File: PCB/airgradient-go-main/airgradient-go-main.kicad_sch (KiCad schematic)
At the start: 200 parts, among them CN1 HCZZ0032-5, CN2 HCZZ0032-5, CN3 HCZZ0032-5, Q1 SIA445EDJ-T1-GE3, Q2 ZVN4106FTA_C508255, Q3 CSD83325L, Q4 SS8050-G, Q5 SI1308EDL, SW1 TS-1091C-A1B3-D2, SW2 TS-1091C-A1B3-D2, U1 W25N512GVEIG, U10 SGP41-D-R4, U11 PS1-CO-SMOKE-10k, U12 SHT4x, U13 SPL07-003, U14 LIS2DH12TR, U15 TMUX121NKGR_C22428404, U16 S12, U17 TCA6408ARGT, U18 TAU1113, U19 LM66200DRLR, U2 ZDSD512MLGEAG, U20 LP5036, U3 BQ27742YZFR-G1, U4 ESP32-C5-MINI-1, U5 BQ25628RYKR, U6 HYG-8503A, U7 TPL5010DDCR, U8 TPS63802DLAR, U9 TPS7A0228DQNR

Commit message: Add 32.768 kHz RTC crystal on IO0/IO1, move ePaper CS to TCA6408A P7
- New RTC 32K block: Y1 Epson FC-135R X1A0001410006 (LCSC C94673,
  CL 6 pF, ESR 50 kOhm max) with C76/C77 8.2 pF C0G (C1579) to PGND,
  on U4 pin 16 (IO0 = XTAL_32K_P) and pin 17 (IO1 = XTAL_32K_N).
- ePaper CS leaves U4 IO0 and moves to expander U17 P7; R39 100K
  pull-up keeps the display deselected while the expander resets.
- design/: requirements, part extraction, intent table and block spec
  (schematic-design skill). net_diff 0 errors, ERC 272 -> 270.
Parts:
- added C76, C77: 8.2pF/50V, Capacitor_SMD:C_0402_1005Metric, symbol Device:C
- added Y1: 32.768kHz CL6pF, Crystal:Crystal_SMD_3215-2Pin_3.2x1.5mm, symbol Device:Crystal
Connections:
- net GND: now also C76.2, C77.2
- net ePaper CS: now also U17.10 (P7); no longer U4.16 (IO0)
- net IO1 renamed XTAL_32K_N
- net XTAL_32K_N: now also C77.1, Y1.2
- new net XTAL_32K_P: C76.1, U4.16 (IO0), Y1.1
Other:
- note added: "RTC 32K"
- note added: "Y1 FC-135R CL 6 pF, ESR 50 kOhm max (FC-135R p2) ESP32-C5 limit ESR <= 70 kOhm (MINI-1 Fig 9-1 p49) C76 = C77 = 2 x (CL - Cstray) = 2 x (6 - 2) = 8.2 pF C0G (R-XT-01) XTAL_32K_P/N = U4 IO0/IO1. ePaper CS moved to U17 P7 (R-XT-02)"

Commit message: Lay out the RTC crystal; move ePaper CS to IO4
Schematic: ePaper CS moves from expander P7 to U4 IO4 (pad 8); P7 gets
an NC flag. The P7 route needed 5 vias through EN_PM1/BUZZ/PRTRG.

PCB (pcb-design skill, groups in design/.../layout/route.json):
- Y1/C77/C76 in the column between U4 and U2, next to U4 pads 16/17.
  XTAL_32K_P/N on F.Cu, 0 vias, 4.9/4.5 mm; C77 GND via 0.5/0.3.
- MOSI rerouted out of that column: U4 trunk -> U1.5 above the
  crystal (1 via), U1.5 -> U2.5 on its right side (2 vias).
- ePaper CS from IO4 under the module body to the old trunk (1 via);
  the old IO0 stub and the dead trunk ends are removed.
- Memory silk line split around the crystal; 8 references re-placed.

Checks: DRC 230 = baseline (0 new), 0 unconnected, parity 0. No new
bends, junctions, dangling ends or vias vs HEAD; unrelated nets
identical to HEAD. Accepted: I2C on B.Cu under Y1/C77 (RF-22, GND
plane between), CS at 0.2 mm.
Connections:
- net IO4 is gone; now on net ePaper CS: U4.8 (IO4)
- net ePaper CS: no longer U17.10 (P7)
- no-connect marks 29 -> 30
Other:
- note added: "Y1 FC-135R CL 6 pF, ESR 50 kOhm max (FC-135R p2) ESP32-C5 limit ESR <= 70 kOhm (MINI-1 Fig 9-1 p49) C76 = C77 = 2 x (CL - Cstray) = 2 x (6 - 2) = 8.2 pF C0G (R-XT-01) XTAL_32K_P/N = U4 IO0/IO1. ePaper CS moved to U4 IO4 (R-XT-02)"
- note removed: "Y1 FC-135R CL 6 pF, ESR 50 kOhm max (FC-135R p2) ESP32-C5 limit ESR <= 70 kOhm (MINI-1 Fig 9-1 p49) C76 = C77 = 2 x (CL - Cstray) = 2 x (6 - 2) = 8.2 pF C0G (R-XT-01) XTAL_32K_P/N = U4 IO0/IO1. ePaper CS moved to U17 P7 (R-XT-02)"
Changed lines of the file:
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@@
 		)
 	)
-	(label "IO4"
+	(label "ePaper CS"
 		(at 120.65 73.66 0)
 		(effects
@@
 		)
 	)
-	(wire
-		(pts
-			(xy 236.22 191.77) (xy 238.76 191.77)
-		)
-		(stroke
-			(width 0)
-			(type default)
-		)
-	)
-	(label "ePaper CS"
-		(at 238.76 191.77 0)
-		(effects
-			(font
-				(size 1.27 1.27)
-			)
-			(justify left bottom)
-		)
+	(no_connect
+		(at 236.22 191.77)
 	)
 	(wire
@@
 		)
 	)
-	(text "Y1 FC-135R CL 6 pF, ESR 50 kOhm max (FC-135R p2)\nESP32-C5 limit ESR <= 70 kOhm (MINI-1 Fig 9-1 p49)\nC76 = C77 = 2 x (CL - Cstray) = 2 x (6 - 2) = 8.2 pF C0G (R-XT-01)\nXTAL_32K_P/N = U4 IO0/IO1. ePaper CS moved to U17 P7 (R-XT-02)"
+	(text "Y1 FC-135R CL 6 pF, ESR 50 kOhm max (FC-135R p2)\nESP32-C5 limit ESR <= 70 kOhm (MINI-1 Fig 9-1 p49)\nC76 = C77 = 2 x (CL - Cstray) = 2 x (6 - 2) = 8.2 pF C0G (R-XT-01)\nXTAL_32K_P/N = U4 IO0/IO1. ePaper CS moved to U4 IO4 (R-XT-02)"
 		(exclude_from_sim no)
 		(at 264.16 370.84 0)

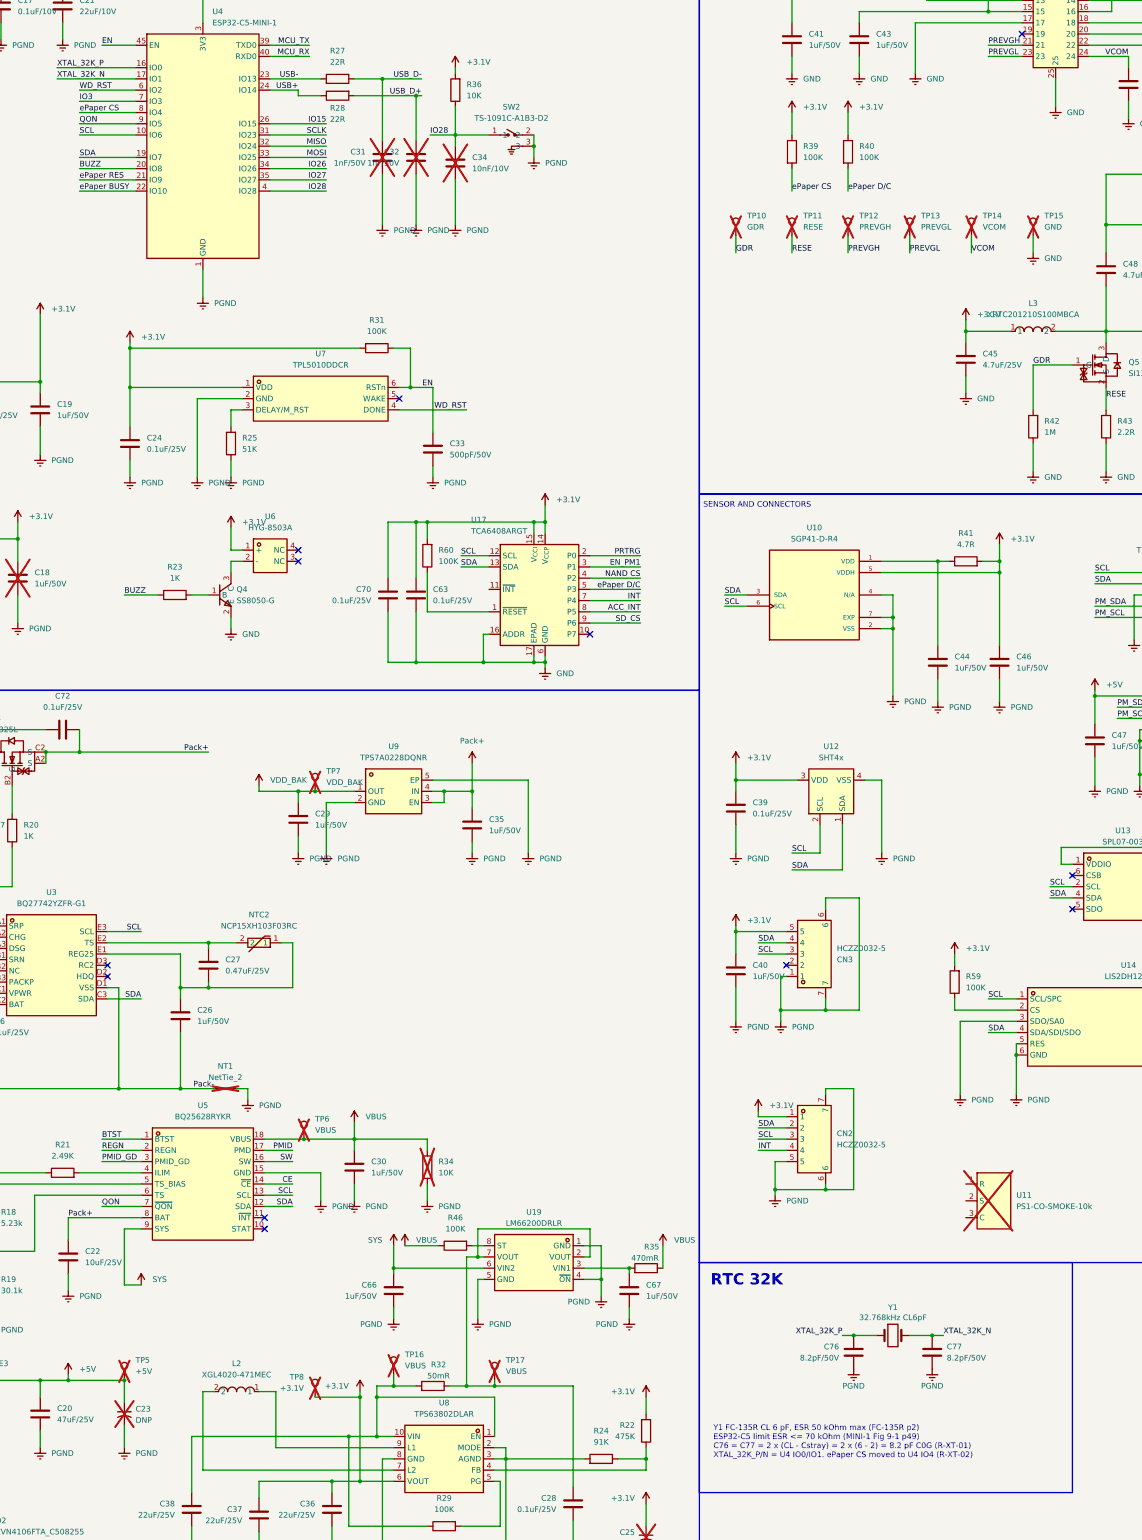
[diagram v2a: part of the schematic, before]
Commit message: Move I2C to the C5 LP I2C pins; WD_RST to IO4, ePaper CS to IO6
The ESP32-C5 LP I2C is fixed to GPIO2 (SDA) and GPIO3 (SCL) by the LP IO
MUX, and v2.1 had the bus on IO6/IO7 (IO7 is not an LP pin). Moving it
lets the LP core read the sensors in offline mode while the HP core
stays in deep sleep (Sam's proposal, R-LP-01..03).

- U4 IO2 = SDA, IO3 = SCL, IO4 = WD_RST (TPL5010 DONE stays on an LP
  pin so the LP core can feed it), IO6 = ePaper CS, IO7 unused.
- WD_RST takes IO4 rather than IO6: from pad 10 the route to U7 needed
  5 vias; from pad 8 it reuses the old CS path with one via.
- Layout: SDA/SCL 2 vias each, WD_RST 1, CS 1, two old vias removed.
  DRC 230 = baseline, 0 unconnected, parity 0; no footprint moved.

Firmware: PIN_I2C_SDA = GPIO2, PIN_I2C_SCL = GPIO3, PIN_EXT_WDT = GPIO4,
PIN_DISPLAY_CS = GPIO6; guard PIN_ACCEL_INT (GPIO3) to V1.
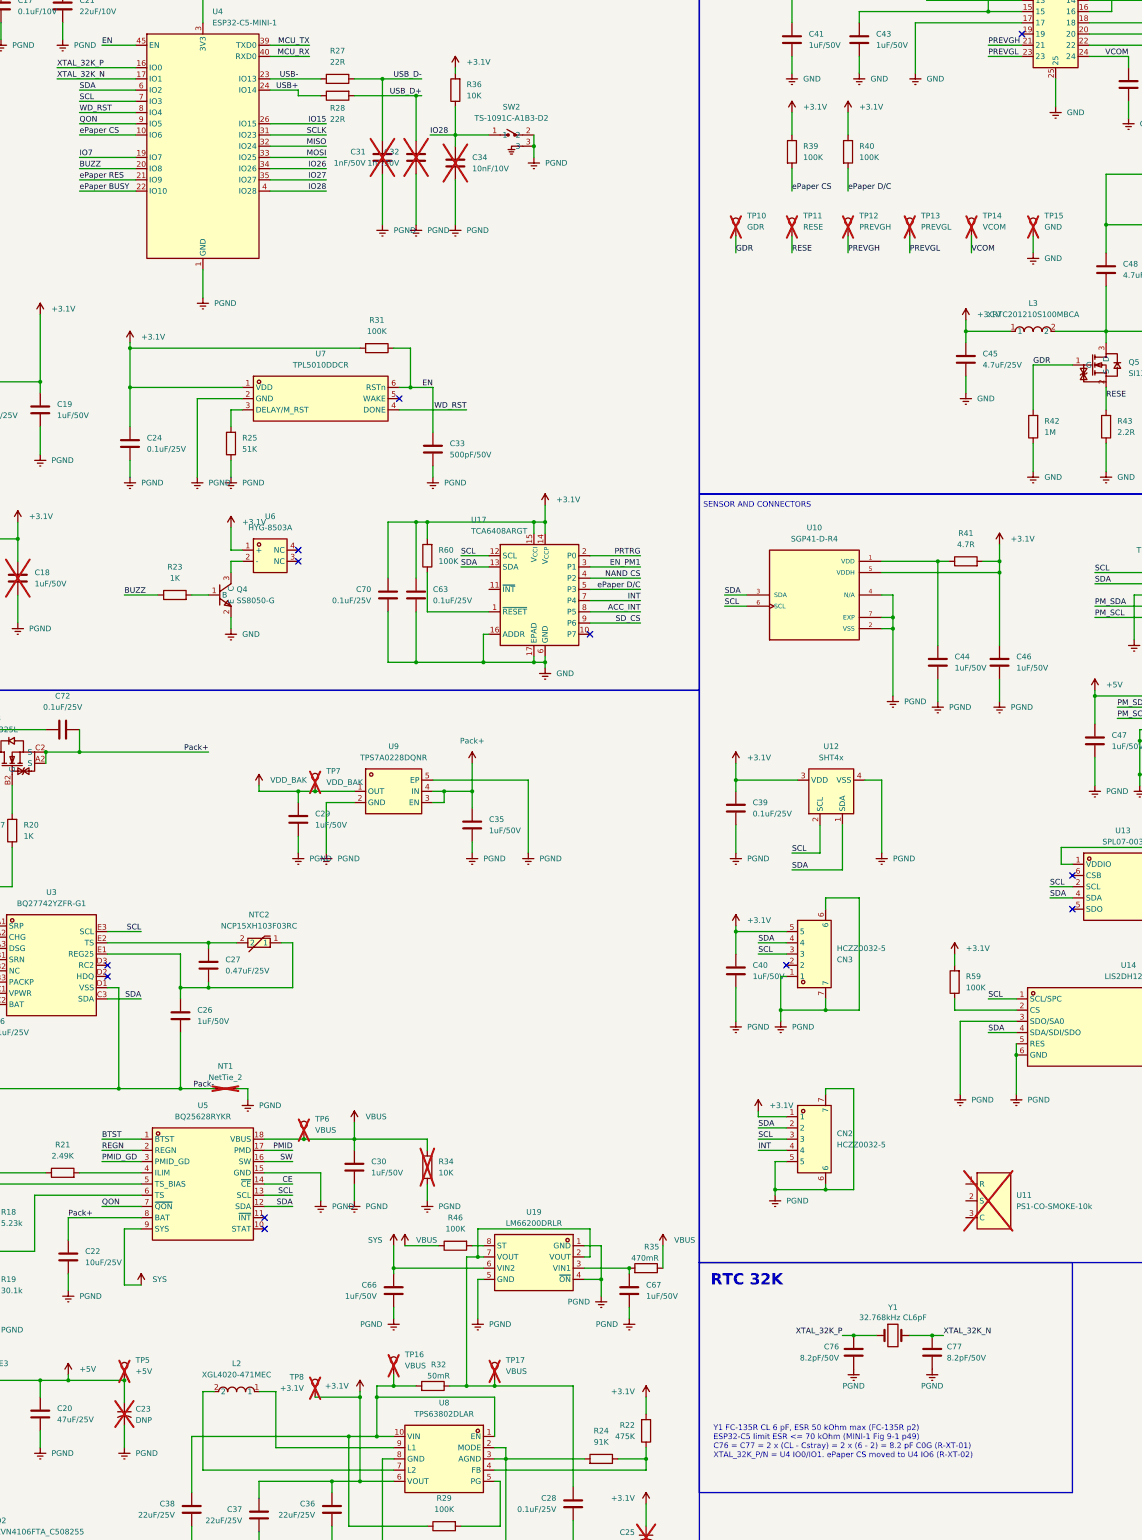
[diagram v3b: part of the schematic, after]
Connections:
- net IO3 is gone; now on net SCL: U4.7 (IO3)
- net SCL: no longer U4.10 (IO6)
- net SDA: now also U4.6 (IO2); no longer U4.19 (IO7)
- net WD_RST: now also U4.8 (IO4); no longer U4.6 (IO2)
- net ePaper CS: now also U4.10 (IO6); no longer U4.8 (IO4)
- new net IO7: U4.19 (IO7)
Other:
- note added: "Y1 FC-135R CL 6 pF, ESR 50 kOhm max (FC-135R p2) ESP32-C5 limit ESR <= 70 kOhm (MINI-1 Fig 9-1 p49) C76 = C77 = 2 x (CL - Cstray) = 2 x (6 - 2) = 8.2 pF C0G (R-XT-01) XTAL_32K_P/N = U4 IO0/IO1. ePaper CS moved to U4 IO6 (R-XT-02)"
- note removed: "Y1 FC-135R CL 6 pF, ESR 50 kOhm max (FC-135R p2) ESP32-C5 limit ESR <= 70 kOhm (MINI-1 Fig 9-1 p49) C76 = C77 = 2 x (CL - Cstray) = 2 x (6 - 2) = 8.2 pF C0G (R-XT-01) XTAL_32K_P/N = U4 IO0/IO1. ePaper CS moved to U4 IO4 (R-XT-02)"
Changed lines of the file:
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@@
 		)
 	)
-	(label "IO3"
+	(label "SCL"
 		(at 120.65 71.12 0)
 		(effects
@@
 		)
 	)
-	(label "SDA"
+	(label "IO7"
 		(at 120.65 83.82 0)
 		(effects
@@
 		)
 	)
-	(label "ePaper CS"
+	(label "WD_RST"
 		(at 120.65 73.66 0)
 		(effects
@@
 		)
 	)
-	(label "SCL"
+	(label "ePaper CS"
 		(at 120.65 78.74 0)
 		(effects
@@
 		)
 	)
-	(label "WD_RST"
+	(label "SDA"
 		(at 120.65 68.58 0)
 		(effects
@@
 		)
 	)
-	(text "Y1 FC-135R CL 6 pF, ESR 50 kOhm max (FC-135R p2)\nESP32-C5 limit ESR <= 70 kOhm (MINI-1 Fig 9-1 p49)\nC76 = C77 = 2 x (CL - Cstray) = 2 x (6 - 2) = 8.2 pF C0G (R-XT-01)\nXTAL_32K_P/N = U4 IO0/IO1. ePaper CS moved to U4 IO4 (R-XT-02)"
+	(text "Y1 FC-135R CL 6 pF, ESR 50 kOhm max (FC-135R p2)\nESP32-C5 limit ESR <= 70 kOhm (MINI-1 Fig 9-1 p49)\nC76 = C77 = 2 x (CL - Cstray) = 2 x (6 - 2) = 8.2 pF C0G (R-XT-01)\nXTAL_32K_P/N = U4 IO0/IO1. ePaper CS moved to U4 IO6 (R-XT-02)"
 		(exclude_from_sim no)
 		(at 264.16 370.84 0)
